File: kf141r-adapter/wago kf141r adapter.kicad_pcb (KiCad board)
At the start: 2 copper layers, 18 x 30 mm, 2 parts, among them J1 Conn_01x10, J2 Conn_01x10

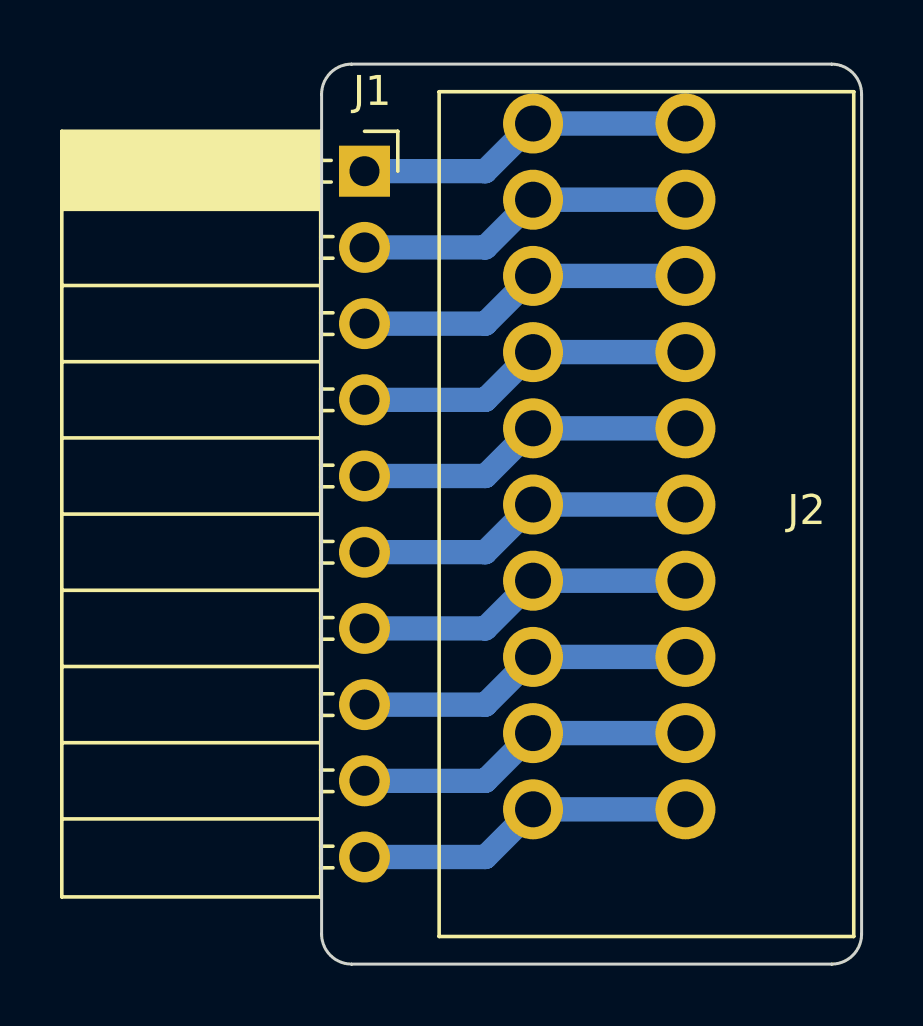
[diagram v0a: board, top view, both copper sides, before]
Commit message: KF141 adapters REV2 - tighter spacing.
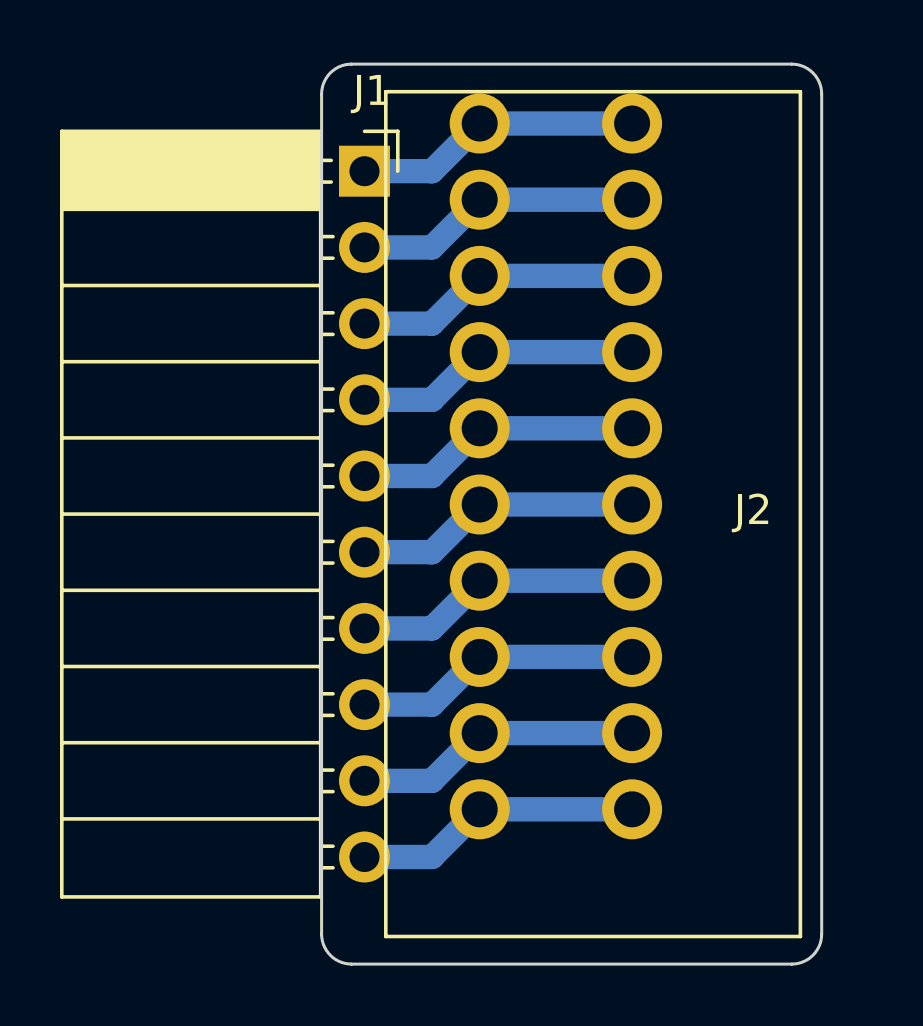
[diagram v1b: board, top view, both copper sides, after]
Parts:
- moved J2 1.78 mm to (146.1, 87.0)
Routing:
- net Net-(J1-Pin_9): track 11.4 -> 9.58 mm
- net Net-(J1-Pin_8): track 11.4 -> 9.58 mm
- net Net-(J1-Pin_7): track 11.4 -> 9.58 mm
- net Net-(J1-Pin_6): track 11.4 -> 9.58 mm
- net Net-(J1-Pin_5): track 11.4 -> 9.58 mm
- net Net-(J1-Pin_4): track 11.4 -> 9.58 mm
- net Net-(J1-Pin_3): track 11.4 -> 9.58 mm
- net Net-(J1-Pin_2): track 11.4 -> 9.58 mm
- net Net-(J1-Pin_10): track 11.4 -> 9.58 mm
- net Net-(J1-Pin_1): track 11.4 -> 9.58 mm
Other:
- board size 18 x 30 mm -> 16.7 x 30 mm
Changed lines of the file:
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@@
       (plotinvisibletext false)
       (sketchpadsonfab false)
-      (subtractmaskfromsilk false)
+      (subtractmaskfromsilk true)
       (outputformat 1)
       (mirror false)
@@
   )
   (footprint "dp_connector:wago_kf141r_2.54" (layer "F.Cu")
-    (at 147.828 87 -90)
+    (at 146.05 87 -90)
     (descr "WAGO KF141 2.54")
     (property "Sheetfile" "wago kf141r adapter.kicad_sch")
@@
       (net 10 "Net-(J1-Pin_10)") (pinfunction "Pin_10") (pintype "passive"))
   )
-  (gr_line (start 138 72) (end 154 72)
-    (stroke (width 0.1) (type default)) (layer "Edge.Cuts"))
-  (gr_line (start 138 102) (end 154 102)
+  (gr_line (start 138 72) (end 152.67 72)
+    (stroke (width 0.1) (type default)) (layer "Edge.Cuts"))
+  (gr_line (start 138 102) (end 152.67 102)
     (stroke (width 0.1) (type default)) (layer "Edge.Cuts"))
   (gr_line (start 137 73) (end 137 101)
     (stroke (width 0.1) (type default)) (layer "Edge.Cuts"))
-  (gr_arc (start 155 101) (mid 154.707107 101.707107) (end 154 102)
-    (stroke (width 0.1) (type default)) (layer "Edge.Cuts"))
-  (gr_arc (start 154 72) (mid 154.707107 72.292893) (end 155 73)
-    (stroke (width 0.1) (type default)) (layer "Edge.Cuts"))
-  (gr_line (start 155 73) (end 155 101)
+  (gr_arc (start 153.67 101) (mid 153.377107 101.707107) (end 152.67 102)
+    (stroke (width 0.1) (type default)) (layer "Edge.Cuts"))
+  (gr_arc (start 152.67 72) (mid 153.377107 72.292893) (end 153.67 73)
+    (stroke (width 0.1) (type default)) (layer "Edge.Cuts"))
+  (gr_line (start 153.67 73) (end 153.67 101)
     (stroke (width 0.1) (type default)) (layer "Edge.Cuts"))
   (gr_arc (start 138 102) (mid 137.292893 101.707107) (end 137 101)
@@
   (gr_arc (start 137 73) (mid 137.292893 72.292893) (end 138 72)
     (stroke (width 0.1) (type default)) (layer "Edge.Cuts"))
-  (segment (start 142.458 75.57) (end 144.048 73.98) (width 0.8128) (layer "B.Cu") (net 1))
-  (segment (start 149.128 73.98) (end 144.048 73.98) (width 0.8128) (layer "B.Cu") (net 1))
-  (segment (start 138.43 75.57) (end 142.458 75.57) (width 0.8128) (layer "B.Cu") (net 1))
-  (segment (start 138.43 78.11) (end 142.458 78.11) (width 0.8128) (layer "B.Cu") (net 2))
-  (segment (start 142.458 78.11) (end 144.048 76.52) (width 0.8128) (layer "B.Cu") (net 2))
-  (segment (start 144.048 76.52) (end 149.128 76.52) (width 0.8128) (layer "B.Cu") (net 2))
-  (segment (start 149.128 79.06) (end 144.048 79.06) (width 0.8128) (layer "B.Cu") (net 3))
-  (segment (start 138.43 80.65) (end 142.458 80.65) (width 0.8128) (layer "B.Cu") (net 3))
-  (segment (start 142.458 80.65) (end 144.048 79.06) (width 0.8128) (layer "B.Cu") (net 3))
-  (segment (start 144.048 81.6) (end 149.128 81.6) (width 0.8128) (layer "B.Cu") (net 4))
-  (segment (start 142.458 83.19) (end 144.048 81.6) (width 0.8128) (layer "B.Cu") (net 4))
-  (segment (start 138.43 83.19) (end 142.458 83.19) (width 0.8128) (layer "B.Cu") (net 4))
-  (segment (start 142.458 85.73) (end 144.048 84.14) (width 0.8128) (layer "B.Cu") (net 5))
-  (segment (start 149.128 84.14) (end 144.048 84.14) (width 0.8128) (layer "B.Cu") (net 5))
-  (segment (start 138.43 85.73) (end 142.458 85.73) (width 0.8128) (layer "B.Cu") (net 5))
-  (segment (start 138.43 88.27) (end 142.458 88.27) (width 0.8128) (layer "B.Cu") (net 6))
-  (segment (start 142.458 88.27) (end 144.048 86.68) (width 0.8128) (layer "B.Cu") (net 6))
-  (segment (start 144.048 86.68) (end 149.128 86.68) (width 0.8128) (layer "B.Cu") (net 6))
-  (segment (start 142.458 90.81) (end 144.048 89.22) (width 0.8128) (layer "B.Cu") (net 7))
-  (segment (start 149.128 89.22) (end 144.048 89.22) (width 0.8128) (layer "B.Cu") (net 7))
-  (segment (start 138.43 90.81) (end 142.458 90.81) (width 0.8128) (layer "B.Cu") (net 7))
-  (segment (start 142.458 93.35) (end 144.048 91.76) (width 0.8128) (layer "B.Cu") (net 8))
-  (segment (start 144.048 91.76) (end 149.128 91.76) (width 0.8128) (layer "B.Cu") (net 8))
-  (segment (start 138.43 93.35) (end 142.458 93.35) (width 0.8128) (layer "B.Cu") (net 8))
-  (segment (start 142.458 95.89) (end 144.048 94.3) (width 0.8128) (layer "B.Cu") (net 9))
-  (segment (start 138.43 95.89) (end 142.458 95.89) (width 0.8128) (layer "B.Cu") (net 9))
-  (segment (start 149.128 94.3) (end 144.048 94.3) (width 0.8128) (layer "B.Cu") (net 9))
-  (segment (start 138.43 98.43) (end 142.458 98.43) (width 0.8128) (layer "B.Cu") (net 10))
-  (segment (start 144.048 96.84) (end 149.128 96.84) (width 0.8128) (layer "B.Cu") (net 10))
-  (segment (start 142.458 98.43) (end 144.048 96.84) (width 0.8128) (layer "B.Cu") (net 10))
+  (segment (start 140.68 75.57) (end 142.27 73.98) (width 0.8128) (layer "B.Cu") (net 1))
+  (segment (start 138.43 75.57) (end 140.68 75.57) (width 0.8128) (layer "B.Cu") (net 1))
+  (segment (start 147.35 73.98) (end 142.27 73.98) (width 0.8128) (layer "B.Cu") (net 1))
+  (segment (start 142.27 76.52) (end 147.35 76.52) (width 0.8128) (layer "B.Cu") (net 2))
+  (segment (start 140.68 78.11) (end 142.27 76.52) (width 0.8128) (layer "B.Cu") (net 2))
+  (segment (start 138.43 78.11) (end 140.68 78.11) (width 0.8128) (layer "B.Cu") (net 2))
+  (segment (start 140.68 80.65) (end 142.27 79.06) (width 0.8128) (layer "B.Cu") (net 3))
+  (segment (start 147.35 79.06) (end 142.27 79.06) (width 0.8128) (layer "B.Cu") (net 3))
+  (segment (start 138.43 80.65) (end 140.68 80.65) (width 0.8128) (layer "B.Cu") (net 3))
+  (segment (start 142.27 81.6) (end 147.35 81.6) (width 0.8128) (layer "B.Cu") (net 4))
+  (segment (start 140.68 83.19) (end 142.27 81.6) (width 0.8128) (layer "B.Cu") (net 4))
+  (segment (start 138.43 83.19) (end 140.68 83.19) (width 0.8128) (layer "B.Cu") (net 4))
+  (segment (start 147.35 84.14) (end 142.27 84.14) (width 0.8128) (layer "B.Cu") (net 5))
+  (segment (start 138.43 85.73) (end 140.68 85.73) (width 0.8128) (layer "B.Cu") (net 5))
+  (segment (start 140.68 85.73) (end 142.27 84.14) (width 0.8128) (layer "B.Cu") (net 5))
+  (segment (start 138.43 88.27) (end 140.68 88.27) (width 0.8128) (layer "B.Cu") (net 6))
+  (segment (start 142.27 86.68) (end 147.35 86.68) (width 0.8128) (layer "B.Cu") (net 6))
+  (segment (start 140.68 88.27) (end 142.27 86.68) (width 0.8128) (layer "B.Cu") (net 6))
+  (segment (start 140.68 90.81) (end 142.27 89.22) (width 0.8128) (layer "B.Cu") (net 7))
+  (segment (start 138.43 90.81) (end 140.68 90.81) (width 0.8128) (layer "B.Cu") (net 7))
+  (segment (start 147.35 89.22) (end 142.27 89.22) (width 0.8128) (layer "B.Cu") (net 7))
+  (segment (start 140.68 93.35) (end 142.27 91.76) (width 0.8128) (layer "B.Cu") (net 8))
+  (segment (start 142.27 91.76) (end 147.35 91.76) (width 0.8128) (layer "B.Cu") (net 8))
+  (segment (start 138.43 93.35) (end 140.68 93.35) (width 0.8128) (layer "B.Cu") (net 8))
+  (segment (start 140.68 95.89) (end 142.27 94.3) (width 0.8128) (layer "B.Cu") (net 9))
+  (segment (start 147.35 94.3) (end 142.27 94.3) (width 0.8128) (layer "B.Cu") (net 9))
+  (segment (start 138.43 95.89) (end 140.68 95.89) (width 0.8128) (layer "B.Cu") (net 9))
+  (segment (start 138.43 98.43) (end 140.68 98.43) (width 0.8128) (layer "B.Cu") (net 10))
+  (segment (start 140.68 98.43) (end 142.27 96.84) (width 0.8128) (layer "B.Cu") (net 10))
+  (segment (start 142.27 96.84) (end 147.35 96.84) (width 0.8128) (layer "B.Cu") (net 10))
 )
